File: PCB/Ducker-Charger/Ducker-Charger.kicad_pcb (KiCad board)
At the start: 2 copper layers, 37 parts, among them IC2 TPS54202HDDCT, IC3 BQ34Z100PWR-R2, J1 Conn_01x02, J6 Debug, Q1 NCE3080K, Q10 AO3400A, Q11 AO3400A, Q12 BC846, Q13 NCE3080K, Q14 NCE3080K, Q2 NCE3080K, Q3 NCE3080K, Q4 NCE3080K, Q5 NCE3080K, Q6 AO4407A, Q7 AO3400A, Q8 AO4407A, Q9 AO3400A, U1 BQ25713RSNR, U1 IP5389_CN_AACD_WC4QD, U2 TPS25750DRJKR, U3 STPD01PUR, U4 TPS54302, U5 INA3221, U6 TPS54302, U7 STM32F401RBT6, U8 BQ7791500PWR, Y1 16MHz

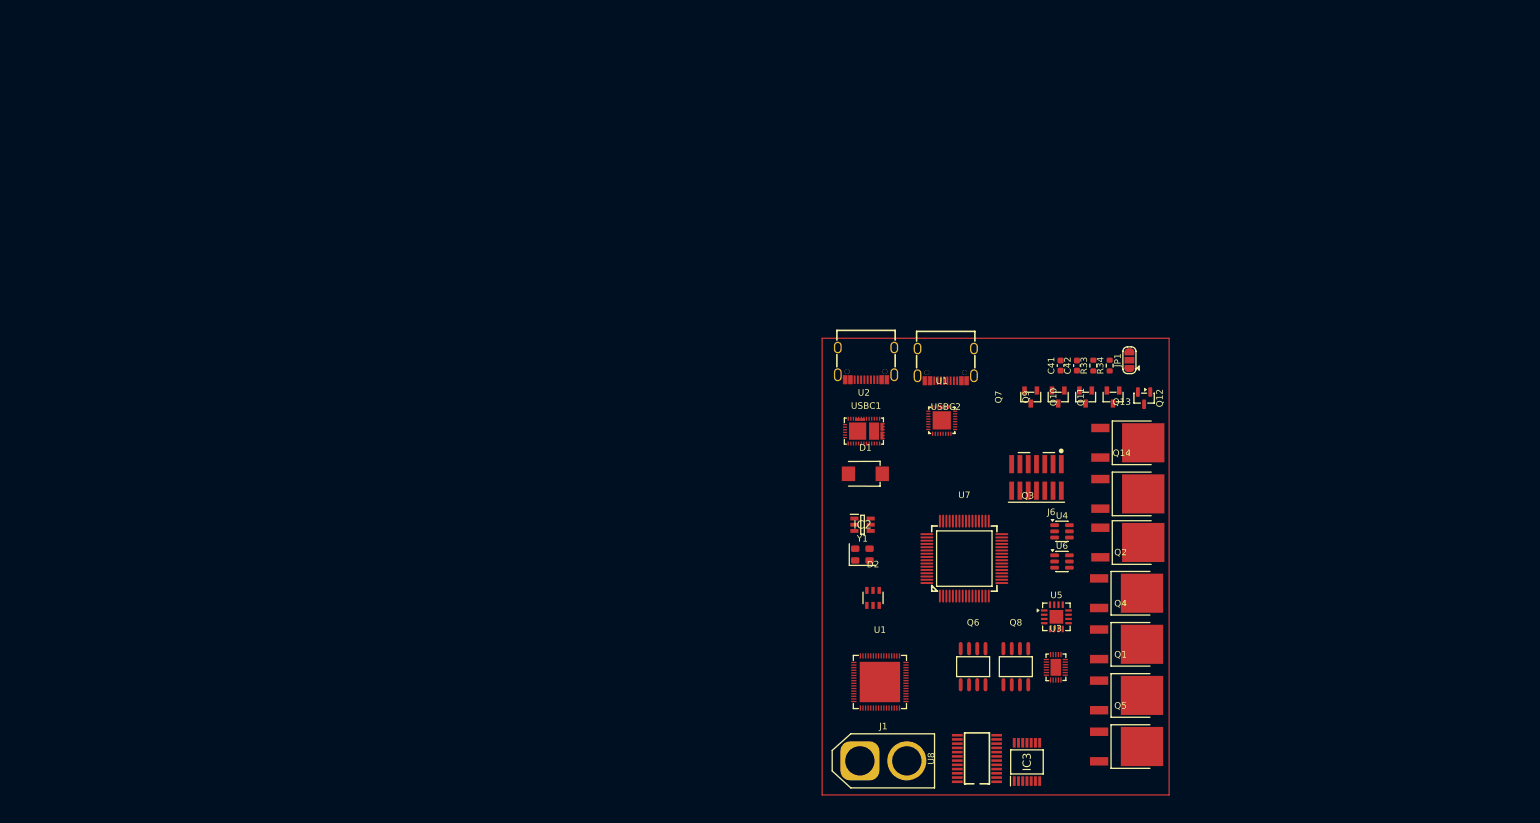
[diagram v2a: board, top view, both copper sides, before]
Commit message: feat: completed BMS section
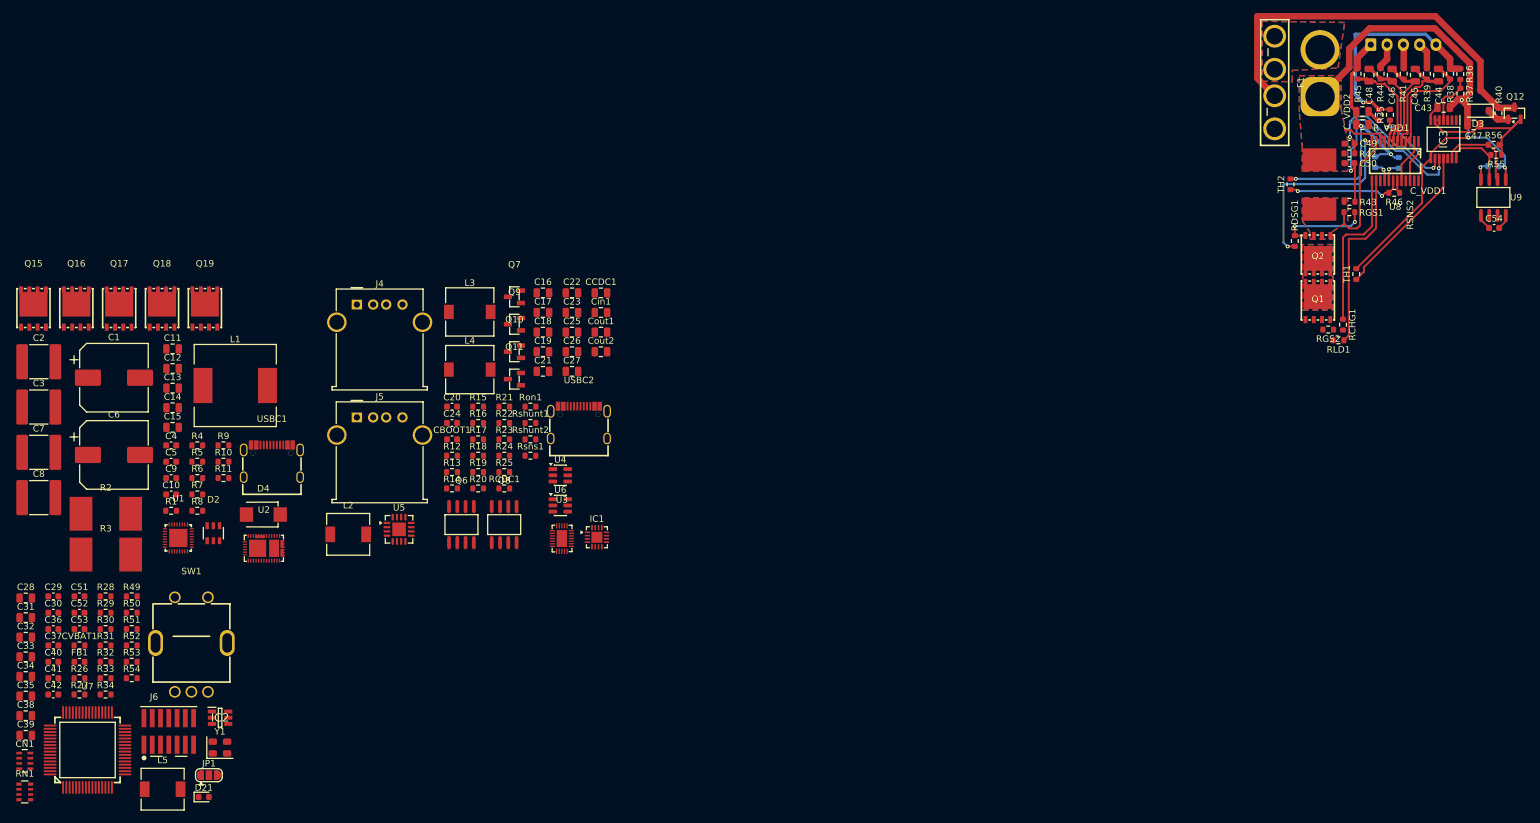
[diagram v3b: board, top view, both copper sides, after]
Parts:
- removed D1: SMBJ22A-E3/52, EasyEDA:SMB_L4.3-W3.6-LS5.4-RD
- removed Q13, Q14, Q3, Q4, Q5: NCE3080K, EasyEDA:TO-252-2_L6.6-W6.1-P4.57-LS9.9-TL-CW
- removed the U1 at (133.7, 79.6)
- removed the U1 at (124.2, 119.7)
- added C1: 220u, Capacitor_SMD:CP_Elec_10x10, F.Cu at (6.65, 73.0)
- added C10: 100n, Capacitor_SMD:C_0603_1608Metric, F.Cu at (15.4, 90.9)
- added C11: 4.7u, Capacitor_SMD:C_0805_2012Metric, F.Cu at (15.6, 68.6)
- added C12: 1u, Capacitor_SMD:C_0805_2012Metric, F.Cu at (15.6, 71.6)
- added C13: 4.7u, Capacitor_SMD:C_0805_2012Metric, F.Cu at (15.6, 74.6)
- added C14: 4.7u, Capacitor_SMD:C_0805_2012Metric, F.Cu at (15.6, 77.6)
- added C15: 4.7u, Capacitor_SMD:C_0805_2012Metric, F.Cu at (15.6, 80.6)
- added C16: 4.7u 50V, Capacitor_SMD:C_0805_2012Metric, F.Cu at (72.5, 60.0)
- added C17: 4.7u 50V, Capacitor_SMD:C_0805_2012Metric, F.Cu at (72.5, 63.0)
- added C18: 1u, Capacitor_SMD:C_0805_2012Metric, F.Cu at (72.5, 66.0)
- added C19: 1u, Capacitor_SMD:C_0805_2012Metric, F.Cu at (72.5, 69.0)
- added C2: 22u, Capacitor_SMD:C_2220_5750Metric, F.Cu at (-4.88, 70.6)
- added C20: 100n, Capacitor_SMD:C_0603_1608Metric, F.Cu at (58.5, 77.5)
- added C21: 10u, Capacitor_SMD:C_0805_2012Metric, F.Cu at (72.5, 72.1)
- added C22: 22u, Capacitor_SMD:C_0805_2012Metric, F.Cu at (76.9, 60.0)
- added C23: 22u, Capacitor_SMD:C_0805_2012Metric, F.Cu at (76.9, 63.0)
- added C24: 100n, Capacitor_SMD:C_0603_1608Metric, F.Cu at (58.5, 80.0)
- added C25: 10u, Capacitor_SMD:C_0805_2012Metric, F.Cu at (76.9, 66.0)
- added C26: 22u, Capacitor_SMD:C_0805_2012Metric, F.Cu at (76.9, 69.0)
- added C27: 22u, Capacitor_SMD:C_0805_2012Metric, F.Cu at (76.9, 72.1)
- added C28: 0.1u, Capacitor_SMD:C_0805_2012Metric, F.Cu at (-6.88, 106.8)
- added C29: 100n, Capacitor_SMD:C_0603_1608Metric, F.Cu at (-2.65, 106.6)
- added C3: 22u, Capacitor_SMD:C_2220_5750Metric, F.Cu at (-4.88, 77.5)
- added C30: 100n, Capacitor_SMD:C_0603_1608Metric, F.Cu at (-2.65, 109.1)
- added C31: 10u, Capacitor_SMD:C_0805_2012Metric, F.Cu at (-6.88, 109.8)
- added C32: 0.1u, Capacitor_SMD:C_0805_2012Metric, F.Cu at (-6.88, 112.8)
- added C33: 22u, Capacitor_SMD:C_0805_2012Metric, F.Cu at (-6.88, 115.9)
- added C34: 22u, Capacitor_SMD:C_0805_2012Metric, F.Cu at (-6.88, 118.9)
- added C35: 75p, Capacitor_SMD:C_0805_2012Metric, F.Cu at (-6.88, 121.9)
- added C36: 100n, Capacitor_SMD:C_0603_1608Metric, F.Cu at (-2.65, 111.6)
- added C37: 100n, Capacitor_SMD:C_0603_1608Metric, F.Cu at (-2.65, 114.1)
- added C38: 2.2u, Capacitor_SMD:C_0805_2012Metric, F.Cu at (-6.88, 124.9)
- added C39: 1u, Capacitor_SMD:C_0805_2012Metric, F.Cu at (-6.88, 127.9)
- added C4: 47n, Capacitor_SMD:C_0603_1608Metric, F.Cu at (15.4, 83.4)
- added C40: 100n, Capacitor_SMD:C_0603_1608Metric, F.Cu at (-2.65, 116.6)
- added C43: 1u, Capacitor_SMD:C_0805_2012Metric, F.Cu at (210.7, 31.6)
- added C44: 1u, Capacitor_SMD:C_0805_2012Metric, F.Cu at (209.9, 26.6)
- added C45: 1u, Capacitor_SMD:C_0805_2012Metric, F.Cu at (206.3, 26.6)
- added C46: 1u, Capacitor_SMD:C_0805_2012Metric, F.Cu at (202.8, 26.6)
- added C47: 4.7u, Capacitor_SMD:C_0805_2012Metric, F.Cu at (215.2, 34.2)
- added C48: 1u, Capacitor_SMD:C_0805_2012Metric, F.Cu at (199.2, 26.6)
- added C49: 100n, Capacitor_SMD:C_0603_1608Metric, F.Cu at (196.2, 37.1)
- added C5: 47n, Capacitor_SMD:C_0603_1608Metric, F.Cu at (15.4, 85.9)
- added C50: 100n, Capacitor_SMD:C_0603_1608Metric, F.Cu at (196.2, 40.1)
- added C51: 100n, Capacitor_SMD:C_0603_1608Metric, F.Cu at (1.35, 106.6)
- added C52: 100n, Capacitor_SMD:C_0603_1608Metric, F.Cu at (1.35, 109.1)
- added C53: 100n, Capacitor_SMD:C_0603_1608Metric, F.Cu at (1.35, 111.6)
- added C54: 100n, Capacitor_SMD:C_0603_1608Metric, F.Cu at (218.4, 50.0)
- added C55: 100n, Capacitor_SMD:C_0603_1608Metric, B.Cu at (218.3, 40.6)
- added C6: 220u, Capacitor_SMD:CP_Elec_10x10, F.Cu at (6.65, 84.9)
- added C7: 22u, Capacitor_SMD:C_2220_5750Metric, F.Cu at (-4.88, 84.5)
- added C8: 22u, Capacitor_SMD:C_2220_5750Metric, F.Cu at (-4.88, 91.4)
- added C9: 100n, Capacitor_SMD:C_0603_1608Metric, F.Cu at (15.4, 88.4)
- added CBOOT1: 100n 50V, Capacitor_SMD:C_0603_1608Metric, F.Cu at (58.5, 82.5)
- added CCDC1: 4.7n, Capacitor_SMD:C_0805_2012Metric, F.Cu at (81.4, 60.0)
- added CN1: C_Pack04, Resistor_SMD:R_Array_Concave_4x0603, F.Cu at (-7.04, 131.8)
- added CVBAT1: 100n, Resistor_SMD:R_0603_1608Metric, F.Cu at (1.35, 114.1)
- added C_VDD1: 1u, Capacitor_SMD:C_0805_2012Metric, F.Cu at (198.2, 32.2)
- added C_VDD2: 1u, Capacitor_SMD:C_0805_2012Metric, F.Cu at (198.2, 34.2)
- added Cin1: 10u 50V, Capacitor_SMD:C_0805_2012Metric, F.Cu at (81.4, 63.0)
- added Cout1: 22u 25V, Capacitor_SMD:C_0805_2012Metric, F.Cu at (81.4, 66.0)
- added Cout2: 22u 25V, Capacitor_SMD:C_0805_2012Metric, F.Cu at (81.4, 69.0)
- added D21: LED, LED_SMD:LED_0603_1608Metric, F.Cu at (20.4, 137.4)
- added D3: D_Zener, Diode_SMD:D_SOD-123, F.Cu at (215.9, 32.1)
- added D4: SMBJ22A-E3/52, EasyEDA:SMB_L4.3-W3.6-LS5.4-RD, F.Cu at (29.6, 94.0)
- added F1: 3522-2, EasyEDA:FUSE-TH_3522-2, F.Cu at (184.7, 27.7)
- added FB1: FerriteBead, Inductor_SMD:L_0603_1608Metric, F.Cu at (1.35, 116.6)
- added IC1: STUSB4710AQ1TR, Package_DFN_QFN:QFN-16-1EP_3x3mm_P0.5mm_EP1.7x1.7mm, F.Cu at (80.7, 97.5)
- added J2: Conn_01x05, Connector_JST:JST_XH_B5B-XH-A_1x05_P2.50mm_Vertical, B.Cu at (199.5, 21.9)
- added J4: USB_A, Connector_USB:USB_A_Molex_67643_Horizontal, F.Cu at (43.9, 61.8)
- added J5: USB_A, Connector_USB:USB_A_Molex_67643_Horizontal, F.Cu at (43.9, 79.1)
- added L1: 2.2u, Inductor_SMD:L_12x12mm_H6mm, F.Cu at (25.3, 74.2)
- added L2: 10u, Inductor_SMD:L_6.3x6.3_H3, F.Cu at (42.6, 97.1)
- added L3: 10u 5A, Inductor_SMD:L_7.3x7.3_H4.5, F.Cu at (61.2, 62.9)
- added L4: 10u 5A, Inductor_SMD:L_7.3x7.3_H4.5, F.Cu at (61.2, 71.8)
- added L5: 10u, Inductor_SMD:L_6.3x6.3_H3, F.Cu at (14.1, 136.2)
- added Q15: BSC040N08NS5, EasyEDA:PG-TDSON-8_L5.9-W5.1-P1.27-LS6.2-BL, F.Cu at (-5.70, 62.4)
- added Q16: BSC040N08NS5, EasyEDA:PG-TDSON-8_L5.9-W5.1-P1.27-LS6.2-BL, F.Cu at (0.88, 62.4)
- added Q17: BSC040N08NS5, EasyEDA:PG-TDSON-8_L5.9-W5.1-P1.27-LS6.2-BL, F.Cu at (7.45, 62.4)
- added Q18: BSC040N08NS5, EasyEDA:PG-TDSON-8_L5.9-W5.1-P1.27-LS6.2-BL, F.Cu at (14.0, 62.4)
- added Q19: BSC040N08NS5, EasyEDA:PG-TDSON-8_L5.9-W5.1-P1.27-LS6.2-BL, F.Cu at (20.6, 62.4)
- added R1: 10, Resistor_SMD:R_0603_1608Metric, F.Cu at (15.4, 93.4)
- added R10: 30k, Resistor_SMD:R_0603_1608Metric, F.Cu at (23.4, 85.9)
- added R11: 10k, Resistor_SMD:R_0603_1608Metric, F.Cu at (23.4, 88.4)
- added R12: 1k2, Resistor_SMD:R_0603_1608Metric, F.Cu at (58.5, 85.0)
- added R13: 50, Resistor_SMD:R_0603_1608Metric, F.Cu at (58.5, 87.5)
- added R14: 100k, Resistor_SMD:R_0603_1608Metric, F.Cu at (58.5, 90.0)
- added R15: 10k, Resistor_SMD:R_0603_1608Metric, F.Cu at (62.5, 77.5)
- added R16: 100k, Resistor_SMD:R_0603_1608Metric, F.Cu at (62.5, 80.0)
- added R17: 10k, Resistor_SMD:R_0603_1608Metric, F.Cu at (62.5, 82.5)
- added R18: 1k, Resistor_SMD:R_0603_1608Metric, F.Cu at (62.5, 85.0)
- added R19: 100k, Resistor_SMD:R_0603_1608Metric, F.Cu at (62.5, 87.5)
- added R2: 5m, EasyEDA:R3920, F.Cu at (5.40, 93.9)
- added R20: 100k, Resistor_SMD:R_0603_1608Metric, F.Cu at (62.5, 90.0)
- added R21: 13.3k, Resistor_SMD:R_0603_1608Metric, F.Cu at (66.5, 77.5)
- added R22: 1k, Resistor_SMD:R_0603_1608Metric, F.Cu at (66.5, 80.0)
- added R23: 100k, Resistor_SMD:R_0603_1608Metric, F.Cu at (66.5, 82.5)
- added R24: 100k, Resistor_SMD:R_0603_1608Metric, F.Cu at (66.5, 85.0)
- added R25: 13.3k, Resistor_SMD:R_0603_1608Metric, F.Cu at (66.5, 87.5)
- added R26: 511k, Resistor_SMD:R_0603_1608Metric, F.Cu at (1.35, 119.1)
- added R27: 100k, Resistor_SMD:R_0603_1608Metric, F.Cu at (1.35, 121.6)
- added R28: 105k, Resistor_SMD:R_0603_1608Metric, F.Cu at (5.37, 106.6)
- added R29: 22.1k, Resistor_SMD:R_0603_1608Metric, F.Cu at (5.37, 109.1)
- added R3: 5m, EasyEDA:R3920, F.Cu at (5.40, 100.2)
- added R30: 0, Resistor_SMD:R_0603_1608Metric, F.Cu at (5.37, 111.6)
- added R31: 4k7, Resistor_SMD:R_0603_1608Metric, F.Cu at (5.37, 114.1)
- added R32: 4k7, Resistor_SMD:R_0603_1608Metric, F.Cu at (5.37, 116.6)
- added R35: 220k, Resistor_SMD:R_0603_1608Metric, F.Cu at (202.4, 32.7)
- added R36: 300k, Resistor_SMD:R_0603_1608Metric, F.Cu at (213.2, 26.4)
- added R37: 16.5k, Resistor_SMD:R_0603_1608Metric, F.Cu at (213.2, 29.4)
- added R38: 1k, Resistor_SMD:R_0603_1608Metric, F.Cu at (211.6, 26.4)
- added R39: 1k, Resistor_SMD:R_0603_1608Metric, F.Cu at (208.1, 26.4)
- added R4: 10, Resistor_SMD:R_0603_1608Metric, F.Cu at (19.4, 83.4)
- added R40: 220k, Resistor_SMD:R_0603_1608Metric, F.Cu at (219.1, 32.5)
- added R41: 1k, Resistor_SMD:R_0603_1608Metric, F.Cu at (204.5, 26.4)
- added R42: 100, Resistor_SMD:R_0603_1608Metric, F.Cu at (196.2, 38.6)
- added R43: 100, Resistor_SMD:R_0603_1608Metric, F.Cu at (196.2, 46.0)
- added R44: 1k, Resistor_SMD:R_0603_1608Metric, F.Cu at (201.0, 26.4)
- added R45: 1k, Resistor_SMD:R_0603_1608Metric, F.Cu at (197.4, 26.4)
- added R46: 10K, Resistor_SMD:R_0603_1608Metric, F.Cu at (203.1, 44.7)
- added R47: 0, Resistor_SMD:R_0603_1608Metric, B.Cu at (200.1, 40.0)
- added R48: 100k, Resistor_SMD:R_0603_1608Metric, B.Cu at (203.8, 40.1)
- added R49: 10k, Resistor_SMD:R_0603_1608Metric, F.Cu at (9.38, 106.6)
- added R5: 10, Resistor_SMD:R_0603_1608Metric, F.Cu at (19.4, 85.9)
- added R50: 10k, Resistor_SMD:R_0603_1608Metric, F.Cu at (9.38, 109.1)
- added R51: 10k, Resistor_SMD:R_0603_1608Metric, F.Cu at (9.38, 111.6)
- added R52: 4k7, Resistor_SMD:R_0603_1608Metric, F.Cu at (9.38, 114.1)
- added R53: 4k7, Resistor_SMD:R_0603_1608Metric, F.Cu at (9.38, 116.6)
- added R54: 1k, Resistor_SMD:R_0603_1608Metric, F.Cu at (9.38, 119.1)
- added R55: 4k7, Resistor_SMD:R_0603_1608Metric, F.Cu at (218.7, 38.8)
- added R56: 4k7, Resistor_SMD:R_0603_1608Metric, F.Cu at (218.3, 37.3)
- added R6: 10, Resistor_SMD:R_0603_1608Metric, F.Cu at (19.4, 88.4)
- added R7: 10, Resistor_SMD:R_0603_1608Metric, F.Cu at (19.4, 90.9)
- added R8: 20k, Resistor_SMD:R_0603_1608Metric, F.Cu at (19.4, 93.4)
- added R9: 10k, Resistor_SMD:R_0603_1608Metric, F.Cu at (23.4, 83.4)
- added RCDC1: 5.6k, Resistor_SMD:R_0603_1608Metric, F.Cu at (66.5, 90.0)
- added RCHG1: 1k, Resistor_SMD:R_0603_1608Metric, F.Cu at (195.2, 64.9)
- added RDSG1: 4k5, Resistor_SMD:R_0603_1608Metric, F.Cu at (187.8, 52.1)
- added RGS1: 1M, Resistor_SMD:R_0603_1608Metric, F.Cu at (196.2, 47.6)
- added RGS2: 1M, Resistor_SMD:R_0603_1608Metric, F.Cu at (192.9, 65.6)
- added RLD1: 470K, Resistor_SMD:R_0603_1608Metric, F.Cu at (194.5, 67.3)
- added RN1: R_Pack04, Resistor_SMD:R_Array_Convex_4x0603, F.Cu at (-7.04, 136.6)
- added RSNS2: 2m, EasyEDA:R3920, F.Cu at (191.6, 43.4)
- added R_VDD1: 1k, Resistor_SMD:R_0603_1608Metric, F.Cu at (200.7, 32.7)
- added Ron1: 100k, Resistor_SMD:R_0603_1608Metric, F.Cu at (70.5, 77.5)
- added Rshunt1: 10m, Resistor_SMD:R_0603_1608Metric, F.Cu at (70.5, 80.0)
- added Rshunt2: 10m, Resistor_SMD:R_0603_1608Metric, F.Cu at (70.5, 82.5)
- added Rsns1: 10m, Resistor_SMD:R_0603_1608Metric, F.Cu at (70.5, 85.0)
- added SW1: EC11E15244G1, EasyEDA:SW-TH_EC11E15244G1, F.Cu at (18.5, 114.0)
- added TH1: 10k, Resistor_SMD:R_0603_1608Metric, F.Cu at (197.2, 57.1)
- added TH2: 10k, Resistor_SMD:R_0603_1608Metric, F.Cu at (187.2, 43.4)
- added U1: BQ25713RSNR, EasyEDA:QFN-32_L4.0-W4.0-P0.40-TL-EP2.8, F.Cu at (16.5, 97.6)
- added U9: ISO1540DR, EasyEDA:SOIC-8_L4.9-W3.9-P1.27-LS6.0-BL, F.Cu at (218.3, 45.4)
- J1: moved to B.Cu
- Q1, Q2: value NCE3080K -> BSC040N08NS5; footprint EasyEDA:TO-252-2_L6.6-W6.1-P4.57-LS9.9-TL-CW -> EasyEDA:PG-TDSON-8_L5.9-W5.1-P1.27-LS6.2-BL
- moved C42 165.0 mm to (-2.65, 121.6), turned to 0 degrees
- moved R34 162.1 mm to (5.37, 121.6), turned to 0 degrees
- moved C41 161.8 mm to (-2.65, 119.1), turned to 0 degrees
- moved R33 158.9 mm to (5.37, 119.1), turned to 0 degrees
- moved JP1 154.9 mm to (21.2, 134.0), turned to 0 degrees
- moved J6 138.7 mm to (15.1, 127.3), turned to 0 degrees
- moved U7 137.7 mm to (2.59, 130.1)
- moved J1 124.0 mm to (191.7, 29.9), turned to 90 degrees
- moved IC3 114.9 mm to (210.6, 36.5), turned to -90 degrees
- moved U8 111.9 mm to (203.2, 39.8), turned to 180 degrees
- moved IC2 102.9 mm to (22.9, 125.2)
- moved Y1 102.9 mm to (22.9, 129.8)
- moved U5 101.7 mm to (50.4, 96.3)
- moved D2 101.7 mm to (21.9, 96.9)
- moved U2 93.8 mm to (29.6, 99.2)
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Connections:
- net /Logic/ADC1_IN4 renamed /Logic/NTC_ONB
- net /Logic/ADC1_IN8 renamed /Logic/CS
- net BATT_- renamed -BATT
- IC2 pad 3: BATT_+ -> +BATT
- IC3 pad 13: SCL -> /BMS/SCL_NOTISO
- IC3 pad 14: SDA -> /BMS/SDA_NOTISO
- J1 pad 2: BATT_+ -> Net-(J1-Pin_2)
- Q1 pad 1: Net-(Q1-G) -> Net-(U8-SRN)
- Q1 pad 2: /High_pow/ACN -> Net-(U8-SRN)
- Q1 pad 3: /High_pow/SW1 -> Net-(U8-SRN)
- Q12 pad 3: BATT_+ -> +BATT
- Q2 pad 1: Net-(Q2-G) -> GND
- Q2 pad 2: /High_pow/V_SYS_A -> GND
- Q2 pad 3: /High_pow/SW2 -> GND
- U2 pad 8: SDA -> /High_pow/I2C_PD.SDA
- U2 pad 9: SCL -> /High_pow/I2C_PD.SCL
- U3 pad 1: SDA -> /BMS/I2C_LP.SDA
- U3 pad 2: SCL -> /BMS/I2C_LP.SCL
- U3 pad 8: BATT_+ -> +BATT
- U3 pad 9: BATT_+ -> +BATT
- U4 pad 3: BATT_+ -> +BATT
- U5 pad 6: SCL -> /BMS/I2C_LP.SCL
- U5 pad 7: SDA -> /BMS/I2C_LP.SDA
- U6 pad 3: BATT_+ -> +BATT
- U7 pad 10: unconnected-(U7-PC2-Pad10) -> USB_A2_CTRL
- U7 pad 11: unconnected-(U7-PC3-Pad11) -> PD_IRQ
- U7 pad 14: /Logic/ADC1_IN0 -> /Logic/NTC_1
- U7 pad 15: /Logic/ADC1_IN1 -> /Logic/NTC_2
- U7 pad 16: /Logic/ADC1_IN2 -> /Logic/NTC_3
- U7 pad 17: /Logic/ADC1_IN3 -> /Logic/NTC_4
- U7 pad 2: unconnected-(U7-PC13-Pad2) -> /Logic/MCU_STATUS
- U7 pad 22: /Logic/ADC1_IN6 -> unconnected-(U7-PA6-Pad22)
- U7 pad 23: /Logic/ADC1_IN7 -> unconnected-(U7-PA7-Pad23)
- U7 pad 27: unconnected-(U7-PB1-Pad27) -> /Logic/DC
- U7 pad 28: unconnected-(U7-PB2-Pad28) -> /Logic/RST
- U7 pad 37: unconnected-(U7-PC6-Pad37) -> /Logic/ENC_A
- U7 pad 38: unconnected-(U7-PC7-Pad38) -> /Logic/ENC_B
- U7 pad 40: unconnected-(U7-PC9-Pad40) -> /High_pow/I2C_PD.SDA
- U7 pad 41: unconnected-(U7-PA8-Pad41) -> /High_pow/I2C_PD.SCL
- U7 pad 58: SCL -> /BMS/I2C_LP.SCL
- U7 pad 59: SDA -> /BMS/I2C_LP.SDA
- U7 pad 60: /Logic/BOOT -> /Logic/BOOT0
- U7 pad 8: unconnected-(U7-PC0-Pad8) -> /Logic/ENC_BUTT
- U7 pad 9: unconnected-(U7-PC1-Pad9) -> USB_A1_CTRL
- U8 pad 11: Net-(Q13-S) -> Net-(U8-SRN)
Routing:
- net -BATT: track 0.00 -> 98.8 mm, vias 0 -> 3
- net +BATT: track 0.00 -> 61.2 mm
- net BATT_SENS_B-: track 0.00 -> 43.2 mm, vias 0 -> 3
- net BATT_SENS_B+: track 0.00 -> 34.7 mm, vias 0 -> 1
- net /BMS/SRN: track 0.00 -> 33.9 mm, vias 0 -> 2
- net Net-(U8-DSG): track 0.00 -> 30.8 mm, vias 0 -> 2
- net Net-(U8-LD): track 0.00 -> 28.0 mm
- net /BMS/REGIN: track 0.00 -> 27.0 mm, vias 0 -> 1
- net Net-(U8-CHG): track 0.00 -> 24.7 mm
- net /BMS/temp: track 0.00 -> 24.1 mm
- net /BMS/SRP: track 0.00 -> 23.2 mm, vias 0 -> 2
- net Net-(U8-SRN): track 0.00 -> 18.6 mm
- net /BMS/VC3: track 0.00 -> 18.2 mm
- net /BMS/TS: track 0.00 -> 17.8 mm, vias 0 -> 2
- net /BMS/VC4: track 0.00 -> 17.6 mm
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- added copper zone on B.Cu, net -BATT
- added copper zone on F.Cu, net -BATT
- added copper zone on In1.Cu, net -BATT
- added copper zone on In2.Cu, net -BATT
- added copper zone on B.Cu, net Net-(J1-Pin_2)
- added copper zone on F.Cu, net Net-(J1-Pin_2)
- added copper zone on In1.Cu, net Net-(J1-Pin_2)
- added copper zone on In2.Cu, net Net-(J1-Pin_2)
- added copper zone on B.Cu, net Net-(Q1-D-Pad5)
- added copper zone on F.Cu, net Net-(Q1-D-Pad5)
- added copper zone on In1.Cu, net Net-(Q1-D-Pad5)
- added copper zone on In2.Cu, net Net-(Q1-D-Pad5)
- added copper zone on B.Cu, net Net-(U8-SRN)
- added copper zone on F.Cu, net Net-(U8-SRN)
- added copper zone on In1.Cu, net Net-(U8-SRN)
- added copper zone on In2.Cu, net Net-(U8-SRN)
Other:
- copper layers 2 -> 4

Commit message: feat: progressed pcb
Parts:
- Rsns1: footprint Resistor_SMD:R_0603_1608Metric -> Resistor_SMD:R_1206_3216Metric
- moved C7 369.5 mm to (362.1, 128.1)
- moved C8 369.5 mm to (362.1, 135.0)
- moved C13 361.1 mm to (367.9, 153.9), turned to 180 degrees
- moved C14 359.0 mm to (365.6, 157.6), turned to 90 degrees
- moved R3 357.8 mm to (362.5, 122.3)
- moved C15 357.1 mm to (365.1, 154.1), turned to 90 degrees
- moved D2 353.4 mm to (371.3, 149.9), turned to -90 degrees
- moved USBC1 352.5 mm to (377.4, 150.3), turned to 90 degrees
- moved C6 349.2 mm to (352.8, 130.8), turned to -90 degrees
- moved U2 345.2 mm to (369.9, 157.5)
- moved D4 340.5 mm to (368.0, 131.2), turned to -90 degrees
- moved Q18 335.4 mm to (343.9, 122.7)
- moved Q19 335.1 mm to (350.4, 121.7), turned to -90 degrees
- moved C5 329.2 mm to (343.0, 118.4), turned to 180 degrees
- moved C2 328.1 mm to (318.2, 127.5)
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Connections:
- C11 pad 1: /High_pow/CELL_CONF -> /High_pow/REGN
- R7 pad 1: /High_pow/CELL_CONF -> /High_pow/REGN
- R8 pad 1: /High_pow/CELL_CONF -> /High_pow/REGN
- R9 pad 1: /High_pow/CELL_CONF -> /High_pow/REGN
- U1 pad 28: /High_pow/CELL_CONF -> /High_pow/REGN
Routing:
- net /High_pow/DP: track 0.00 -> 17.8 mm, vias 0 -> 2
- net /High_pow/CC2: track 0.00 -> 15.3 mm
- net /High_pow/DN: track 0.00 -> 14.5 mm, vias 0 -> 2
- net /High_pow/LODRV2: track 0.00 -> 12.1 mm
- net /High_pow/CC1: track 0.00 -> 8.32 mm, vias 0 -> 2
- net Net-(Q7-G): track 0.00 -> 6.98 mm
- net /High_pow/ACP: track 0.00 -> 6.76 mm
- net /Low_pow/VBUS: track 0.00 -> 3.81 mm
- net Net-(Q2-G): track 0.00 -> 3.22 mm
- net Net-(Q6-G): track 0.00 -> 3.20 mm
- net GND: track 2.32 -> 5.21 mm
- net /High_pow/LDO_3V3: track 0.00 -> 2.45 mm
- net /High_pow/BTST1: track 0.00 -> 2.38 mm
- net /High_pow/BTST2: track 0.00 -> 2.20 mm
- net Net-(U3-BOOT): track 0.00 -> 1.83 mm
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- added copper zone on In2.Cu, net +3V3
- added copper zone on B.Cu, net +BATT
- added copper zone on F.Cu, net +BATT
- added copper zone on In1.Cu, net +BATT
- added copper zone on In2.Cu, net +BATT
- added copper zone on B.Cu, net /High_pow/ACN
- added copper zone on F.Cu, net /High_pow/ACN
- added copper zone on In1.Cu, net /High_pow/ACN
- added copper zone on In2.Cu, net /High_pow/ACN
- added copper zone on B.Cu, net /High_pow/SW1
- added copper zone on F.Cu, net /High_pow/SW1
- added copper zone on In1.Cu, net /High_pow/SW1
- added copper zone on In2.Cu, net /High_pow/SW1
- added copper zone on B.Cu, net /High_pow/SW2
- added copper zone on F.Cu, net /High_pow/SW2
- added copper zone on In1.Cu, net /High_pow/SW2
- added copper zone on In2.Cu, net /High_pow/SW2
- added copper zone on B.Cu, net /High_pow/V_SYS_A
- added copper zone on F.Cu, net /High_pow/V_SYS_A
- added copper zone on In1.Cu, net /High_pow/V_SYS_A
- added copper zone on In2.Cu, net /High_pow/V_SYS_A
- added copper zone on B.Cu, net /High_pow/V_SYS_B
- added copper zone on F.Cu, net /High_pow/V_SYS_B
- added copper zone on In1.Cu, net /High_pow/V_SYS_B
- added copper zone on In2.Cu, net /High_pow/V_SYS_B
- added copper zone on In1.Cu, net GND
- added copper zone on B.Cu, net Net-(CBOOT1-Pad2)
- added copper zone on F.Cu, net Net-(CBOOT1-Pad2)
- added copper zone on In1.Cu, net Net-(CBOOT1-Pad2)
- added copper zone on In2.Cu, net Net-(CBOOT1-Pad2)
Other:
- board outline added: 65 x 100.4 mm

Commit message: feat: PCB v1.0 is now ready
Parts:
- added C56: 1u, Capacitor_SMD:C_0603_1608Metric, F.Cu at (180.9, 118.6)
- added G***: LOGO, LOGO, F.Cu at (220.1, 25.0)
- added G***: LOGO, LOGO, B.Cu at (196.2, 81.2)
- added J3: Conn_01x02, TestPoint:TestPoint_Bridge_Pitch6.35mm_Drill1.3mm, F.Cu at (198.0, 109.3)
- added J7: Conn_01x08, Connector_FFC-FPC:Molex_200528-0080_1x08-1MP_P1.00mm_Horizontal, B.Cu at (222.1, 43.7)
- added J8: Conn_01x07, Connector_JST:JST_XH_S7B-XH-A_1x07_P2.50mm_Horizontal, B.Cu at (218.7, 56.9)
- added R57: 10, Resistor_SMD:R_0603_1608Metric, F.Cu at (178.6, 118.0)
- added kibuzzard-694FF1FC: G***, kibuzzard-694FF1FC, F.Cu at (193.3, 21.8)
- added kibuzzard-694FF21A: G***, kibuzzard-694FF21A, F.Cu at (190.9, 21.8)
- added kibuzzard-694FF228: G***, kibuzzard-694FF228, F.Cu at (195.9, 21.8)
- added kibuzzard-694FF236: G***, kibuzzard-694FF236, F.Cu at (198.6, 21.8)
- added kibuzzard-694FF248: G***, kibuzzard-694FF248, F.Cu at (201.0, 21.8)
- C29, C30, C36, C37, C38, C39, C4, C40, C5, C51, C52, C53, CVBAT1, FB1, R49, R50, R51, R52, R53: moved to B.Cu
- Rshunt1, Rshunt2: footprint Resistor_SMD:R_0603_1608Metric -> Resistor_SMD:R_1206_3216Metric
- moved RN1 280.1 mm to (225.2, 61.9)
- moved CN1 277.1 mm to (225.2, 66.8)
- moved C53 274.4 mm to (221.7, 21.6), turned to -90 degrees
- moved R32 273.0 mm to (227.2, 34.1), turned to -90 degrees
- moved C52 272.1 mm to (223.6, 30.0), turned to 90 degrees
- moved R31 269.9 mm to (224.8, 34.1), turned to -90 degrees
- moved R51 268.4 mm to (223.2, 21.6), turned to 90 degrees
- moved C38 266.3 mm to (212.8, 55.9)
- moved C51 263.6 mm to (215.5, 30.0), turned to 90 degrees
- moved R50 263.2 mm to (222.1, 30.0), turned to -90 degrees
- moved C39 262.1 mm to (210.1, 64.2), turned to 135 degrees
- moved J6 260.7 mm to (223.6, 44.3), turned to 180 degrees
- moved C41 257.9 mm to (215.4, 74.9), turned to -135 degrees
- moved R49 257.5 mm to (217.0, 30.0), turned to -90 degrees
- moved SW1 255.8 mm to (219.5, 25.8)
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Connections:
- CN1 pad 5: /Logic/NTC_4 -> /Logic/NTC_1
- CN1 pad 6: /Logic/NTC_3 -> /Logic/NTC_2
- CN1 pad 7: /Logic/NTC_2 -> /Logic/NTC_3
- CN1 pad 8: /Logic/NTC_1 -> /Logic/NTC_4
- IC1 pad 1: +BATT -> Net-(IC1-VDD)
- IC1 pad 17: (no net) -> GND
- R15 pad 1: /Low_pow/USB_C_2ENABLER -> /Logic/LAB_2ENABLER
- R17 pad 1: /Low_pow/LAB_2ENABLER -> /Logic/USB_C_2ENABLER
- RN1 pad 1: /Logic/NTC_1 -> /Logic/NTC_4
- RN1 pad 2: /Logic/NTC_2 -> /Logic/NTC_3
- RN1 pad 3: /Logic/NTC_3 -> /Logic/NTC_2
- RN1 pad 4: /Logic/NTC_4 -> /Logic/NTC_1
- U3 pad 4: /Low_pow/LP_ST_INT -> LP_ST_INT
- U3 pad 5: /Low_pow/LP_ST_EN -> LP_ST_EN
- U7 pad 23: unconnected-(U7-PA7-Pad23) -> /Logic/SPI1_MOSI
- U7 pad 44: unconnected-(U7-PA11-Pad44) -> /Logic/LAB_2ENABLER
- U7 pad 45: unconnected-(U7-PA12-Pad45) -> /Logic/USB_C_2ENABLER
- U7 pad 50: /Logic/TIM2_CH1 -> unconnected-(U7-PA15-Pad50)
- U7 pad 52: unconnected-(U7-PC11-Pad52) -> LP_ST_EN
- U7 pad 53: unconnected-(U7-PC12-Pad53) -> LP_ST_INT
- U7 pad 57: /Logic/SPI1_MOSI -> unconnected-(U7-PB5-Pad57)
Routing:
- net GND: track 5.21 -> 162.0 mm, vias 0 -> 159
- net /BMS/I2C_LP.SCL: track 0.00 -> 144.1 mm, vias 0 -> 7
- net /BMS/I2C_LP.SDA: track 0.00 -> 143.0 mm, vias 0 -> 7
- net /High_pow/I2C_PD.SDA: track 0.00 -> 124.6 mm, vias 0 -> 3
- net /High_pow/I2C_PD.SCL: track 0.00 -> 122.9 mm, vias 0 -> 2
- net /Logic/LAB_2ENABLER: track 0.00 -> 115.0 mm, vias 0 -> 2
- net PD_IRQ: track 0.00 -> 91.4 mm, vias 0 -> 4
- net /Logic/ENC_BUTT: track 0.00 -> 66.8 mm, vias 0 -> 2
- net Net-(Q18-G): track 0.00 -> 65.6 mm
- net /Low_pow/CC2: track 0.00 -> 64.0 mm, vias 0 -> 2
- net /Logic/USB_C_2ENABLER: track 0.00 -> 61.7 mm, vias 0 -> 2
- net /Logic/NTC_4: track 0.00 -> 59.7 mm, vias 0 -> 2
- net /Logic/~{RESET}: track 0.00 -> 59.0 mm, vias 0 -> 2
- net /Low_pow/CC1: track 0.00 -> 58.9 mm, vias 0 -> 2
- net /High_pow/SW1: track 1.41 -> 59.0 mm, vias 0 -> 3
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- added copper zone on F.Cu, net +3V3
- added copper zone on B.Cu, net /High_pow/ACP
- added copper zone on F.Cu, net /High_pow/ACP
- added copper zone on F.Cu, net /Low_pow/5V_USB_A1
- added copper zone on F.Cu, net /Low_pow/5V_USB_A2
- added copper zone on F.Cu, net /Low_pow/IN-1
- added copper zone on F.Cu, net /Low_pow/IN-2
- added copper zone on F.Cu, net /Low_pow/VBUS
- added copper zone on B.Cu, net /Low_pow/V_LABS
- added copper zone on F.Cu, net /Low_pow/V_LABS
- added copper zone on In1.Cu, net /Low_pow/V_LABS
- added copper zone on In2.Cu, net /Low_pow/V_LABS
- added copper zone on F.Cu, net /Low_pow/V_OUT_AUX
- added copper zone on B.Cu, net GND
- added copper zone on F.Cu, net GND
- removed copper zone on B.Cu, net Net-(CBOOT1-Pad2)
- removed copper zone on In1.Cu, net Net-(CBOOT1-Pad2)
- removed copper zone on In2.Cu, net Net-(CBOOT1-Pad2)
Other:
- board size 65 x 100.4 mm -> 61.8 x 130.1 mm
